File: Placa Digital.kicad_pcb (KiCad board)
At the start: 2 copper layers, 60 x 80 mm, 23 parts, among them J1 Entradas / Salidas, Q1 BC548, Q2 BC548, U1 EC11_Module, U2 Alimentación, U3 ST7920_Display, U4 10K

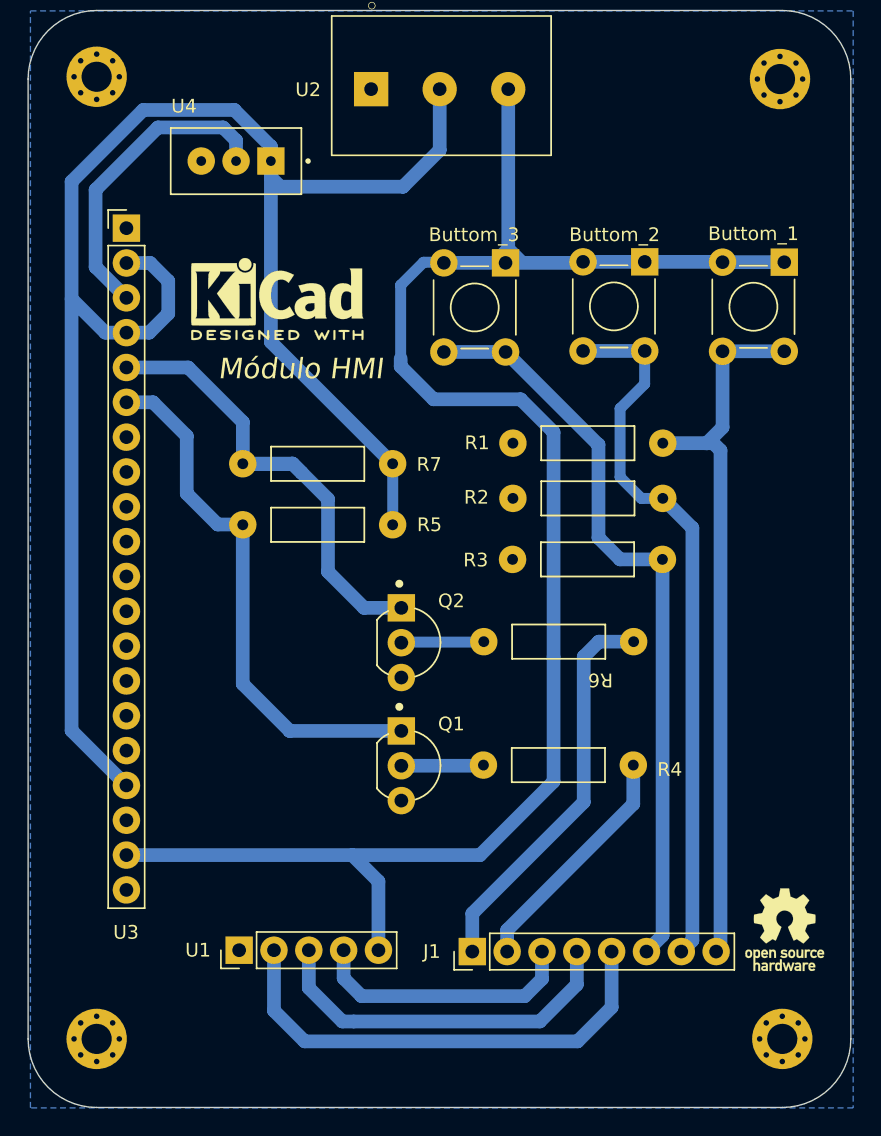
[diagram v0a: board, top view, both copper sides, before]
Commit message: Button changed
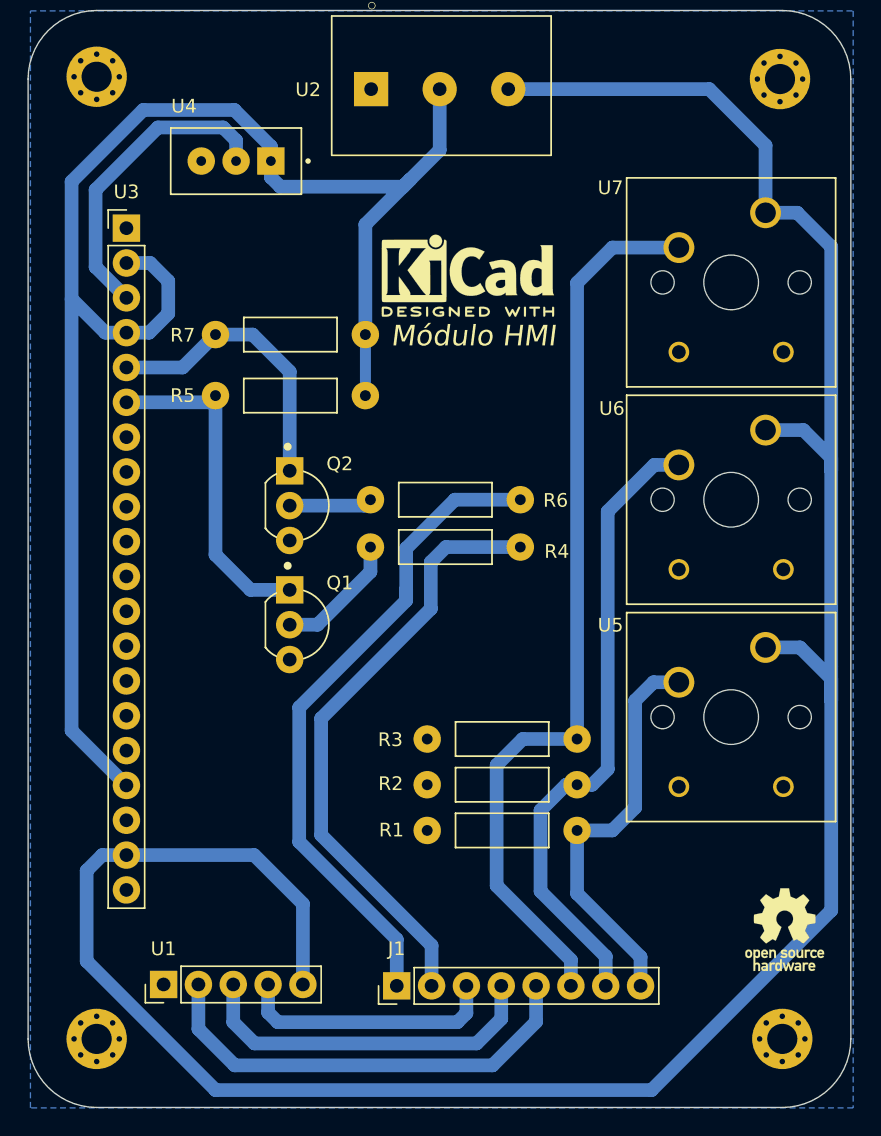
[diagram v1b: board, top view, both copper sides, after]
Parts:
- removed Buttom_1, Buttom_2, Buttom_3: -, CEDCp:Pulsador_4Pines
- added U5: MX1A-11NN, CEDCp:CHERRY_MX1A-11NN_SWITCH, F.Cu at (161.7, 110.8)
- added U6: MX1A-11NN, CEDCp:CHERRY_MX1A-11NN_SWITCH, F.Cu at (161.7, 95.0)
- added U7: MX1A-11NN, CEDCp:CHERRY_MX1A-11NN_SWITCH, F.Cu at (161.7, 79.1)
- moved R1 28.9 mm to (145.0, 119.1)
- moved R2 21.8 mm to (145.0, 115.8)
- moved R4 17.9 mm to (140.9, 98.4)
- moved R3 14.5 mm to (145.0, 112.4)
- moved REF** 14.0 mm to (142.5, 78.6)
- moved R6 13.2 mm to (140.9, 95.0)
- moved Q1 13.1 mm to (130.4, 104.1)
- moved Q2 12.9 mm to (130.4, 95.4)
- moved R5 9.63 mm to (129.6, 87.4)
- moved R7 9.63 mm to (129.6, 82.9)
- moved J1 6.05 mm to (137.3, 130.4)
- moved U1 6.05 mm to (120.3, 130.3)
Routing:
- net /toMicroC_Button1: track 67.7 -> 29.7 mm
- net Net-(Q1-Pad1): track 65.7 -> 36.4 mm
- net /fromMicroC_DisplaySCLK: track 17.4 -> 44.5 mm
- net Net-(Q2-Pad1): track 46.2 -> 21.3 mm
- net /fromMicroC_DisplaySID: track 31.5 -> 48.6 mm
- net +5V: track 175.3 -> 158.8 mm
- net +3V3: track 198.0 -> 187.3 mm
- net /toMicroC_Button2: track 56.9 -> 46.3 mm
- net Net-(Q1-Pad2): track 12.0 -> 9.29 mm
- net /toMicroC_Button3: track 69.4 -> 66.8 mm
- net /toMicroC_EncoderSignalA: track 35.1 -> 32.9 mm
- net /toMicroC_EncoderSignalB: track 26.8 -> 26.1 mm

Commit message: Last version
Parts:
- added H1: MountingHole, MountingHole:MountingHole_2.2mm_M2_Pad_Via, F.Cu at (142.3, 26.4)
- added H1: MountingHole, MountingHole:MountingHole_2.2mm_M2_Pad_Via, F.Cu at (40.1, 118.9)
- added H1: MountingHole, MountingHole:MountingHole_2.2mm_M2_Pad_Via, F.Cu at (142.6, 119.2)
- added H2: MountingHole, MountingHole:MountingHole_2.2mm_M2_Pad_Via, F.Cu at (90.0, 119.1)
- added H2: MountingHole, MountingHole:MountingHole_2.2mm_M2_Pad_Via, F.Cu at (192.1, 26.6)
- added H2: MountingHole, MountingHole:MountingHole_2.2mm_M2_Pad_Via, F.Cu at (192.5, 119.4)
- added H3: MountingHole, MountingHole:MountingHole_2.2mm_M2_Pad_Via, F.Cu at (192.6, 189.4)
- added H3: MountingHole, MountingHole:MountingHole_2.2mm_M2_Pad_Via, F.Cu at (192.3, 96.6)
- added H3: MountingHole, MountingHole:MountingHole_2.2mm_M2_Pad_Via, F.Cu at (90.1, 189.1)
- added H4: MountingHole, MountingHole:MountingHole_2.2mm_M2_Pad_Via, F.Cu at (142.6, 189.4)
- added H4: MountingHole, MountingHole:MountingHole_2.2mm_M2_Pad_Via, F.Cu at (142.3, 96.6)
- added H4: MountingHole, MountingHole:MountingHole_2.2mm_M2_Pad_Via, F.Cu at (40.1, 189.1)
- added J1: Entradas / Salidas, Connector_PinHeader_2.54mm:PinHeader_1x08_P2.54mm_Vertical, F.Cu at (62.0, 185.2)
- added J1: Entradas / Salidas, Connector_PinHeader_2.54mm:PinHeader_1x08_P2.54mm_Vertical, F.Cu at (164.2, 92.7)
- added J1: Entradas / Salidas, Connector_PinHeader_2.54mm:PinHeader_1x08_P2.54mm_Vertical, F.Cu at (164.5, 185.5)
- added Q1: BC548, CEDCp:BC548, F.Cu at (157.6, 159.2)
- added Q1: BC548, CEDCp:BC548, F.Cu at (157.2, 66.4)
- added Q1: BC548, CEDCp:BC548, F.Cu at (55.1, 158.9)
- added Q2: BC548, CEDCp:BC548, F.Cu at (55.1, 150.2)
- added Q2: BC548, CEDCp:BC548, F.Cu at (157.6, 150.5)
- added Q2: BC548, CEDCp:BC548, F.Cu at (157.2, 57.7)
- added R1: 10k, CEDCp:Resistencia_0,25W, F.Cu at (172.2, 174.2)
- added R1: 10k, CEDCp:Resistencia_0,25W, F.Cu at (171.8, 81.4)
- added R1: 10k, CEDCp:Resistencia_0,25W, F.Cu at (69.7, 173.9)
- added R2: 10k, CEDCp:Resistencia_0,25W, F.Cu at (171.8, 78.1)
- added R2: 10k, CEDCp:Resistencia_0,25W, F.Cu at (69.7, 170.5)
- added R2: 10k, CEDCp:Resistencia_0,25W, F.Cu at (172.2, 170.9)
- added R3: 10k, CEDCp:Resistencia_0,25W, F.Cu at (69.7, 167.2)
- added R3: 10k, CEDCp:Resistencia_0,25W, F.Cu at (172.2, 167.5)
- added R3: 10k, CEDCp:Resistencia_0,25W, F.Cu at (171.8, 74.7)
- added R4: 2k7, CEDCp:Resistencia_0,25W, F.Cu at (168.1, 153.5)
- added R4: 2k7, CEDCp:Resistencia_0,25W, F.Cu at (167.7, 60.7)
- added R4: 2k7, CEDCp:Resistencia_0,25W, F.Cu at (65.6, 153.2)
- added R5: 1k, CEDCp:Resistencia_0,25W, F.Cu at (54.3, 142.1)
- added R5: 1k, CEDCp:Resistencia_0,25W, F.Cu at (156.8, 142.5)
- added R5: 1k, CEDCp:Resistencia_0,25W, F.Cu at (156.4, 49.7)
- added R6: 2k7, CEDCp:Resistencia_0,25W, F.Cu at (167.7, 57.3)
- added R6: 2k7, CEDCp:Resistencia_0,25W, F.Cu at (65.6, 149.7)
- added R6: 2k7, CEDCp:Resistencia_0,25W, F.Cu at (168.1, 150.1)
- added R7: 1k, CEDCp:Resistencia_0,25W, F.Cu at (156.4, 45.2)
- added R7: 1k, CEDCp:Resistencia_0,25W, F.Cu at (54.3, 137.7)
- added R7: 1k, CEDCp:Resistencia_0,25W, F.Cu at (156.8, 138.0)
- added REF**: KiCad-Logo2_5mm_SilkScreen, Symbol:KiCad-Logo2_5mm_SilkScreen, F.Cu at (67.2, 133.4)
- added REF**: OSHW-Logo_5.7x6mm_SilkScreen, Symbol:OSHW-Logo_5.7x6mm_SilkScreen, F.Cu at (90.3, 181.1)
- added REF**: KiCad-Logo2_5mm_SilkScreen, Symbol:KiCad-Logo2_5mm_SilkScreen, F.Cu at (169.3, 40.9)
- added REF**: KiCad-Logo2_5mm_SilkScreen, Symbol:KiCad-Logo2_5mm_SilkScreen, F.Cu at (169.7, 133.7)
- added REF**: OSHW-Logo_5.7x6mm_SilkScreen, Symbol:OSHW-Logo_5.7x6mm_SilkScreen, F.Cu at (192.4, 88.6)
- added REF**: OSHW-Logo_5.7x6mm_SilkScreen, Symbol:OSHW-Logo_5.7x6mm_SilkScreen, F.Cu at (192.8, 181.4)
- added U1: EC11_Module, Connector_PinHeader_2.54mm:PinHeader_1x05_P2.54mm_Vertical, F.Cu at (45.0, 185.1)
- added U1: EC11_Module, Connector_PinHeader_2.54mm:PinHeader_1x05_P2.54mm_Vertical, F.Cu at (147.2, 92.6)
- added U1: EC11_Module, Connector_PinHeader_2.54mm:PinHeader_1x05_P2.54mm_Vertical, F.Cu at (147.5, 185.4)
- added U2: Alimentación, CEDCp:Bornera_1x3, F.Cu at (167.7, 120.1)
- added U2: Alimentación, CEDCp:Bornera_1x3, F.Cu at (65.1, 119.8)
- added U2: Alimentación, CEDCp:Bornera_1x3, F.Cu at (167.3, 27.3)
- added U3: ST7920_Display, Connector_PinHeader_2.54mm:PinHeader_1x20_P2.54mm_Vertical, F.Cu at (144.4, 37.5)
- added U3: ST7920_Display, Connector_PinHeader_2.54mm:PinHeader_1x20_P2.54mm_Vertical, F.Cu at (42.3, 129.9)
- added U3: ST7920_Display, Connector_PinHeader_2.54mm:PinHeader_1x20_P2.54mm_Vertical, F.Cu at (144.8, 130.3)
- added U4: 10K, CEDCp:Preset_Multivueltas_Vertical, F.Cu at (152.4, 32.6)
- added U4: 10K, CEDCp:Preset_Multivueltas_Vertical, F.Cu at (50.3, 125.0)
- added U4: 10K, CEDCp:Preset_Multivueltas_Vertical, F.Cu at (152.8, 125.4)
- added U5: MX1A-11NN, CEDCp:CHERRY_MX1A-11NN_SWITCH, B.Cu at (188.5, 73.1)
- added U5: MX1A-11NN, CEDCp:CHERRY_MX1A-11NN_SWITCH, B.Cu at (86.4, 165.6)
- added U5: MX1A-11NN, CEDCp:CHERRY_MX1A-11NN_SWITCH, B.Cu at (188.9, 165.9)
- added U6: MX1A-11NN, CEDCp:CHERRY_MX1A-11NN_SWITCH, B.Cu at (188.5, 57.3)
- added U6: MX1A-11NN, CEDCp:CHERRY_MX1A-11NN_SWITCH, B.Cu at (86.4, 149.7)
- added U6: MX1A-11NN, CEDCp:CHERRY_MX1A-11NN_SWITCH, B.Cu at (188.9, 150.1)
- added U7: MX1A-11NN, CEDCp:CHERRY_MX1A-11NN_SWITCH, B.Cu at (188.5, 41.4)
- added U7: MX1A-11NN, CEDCp:CHERRY_MX1A-11NN_SWITCH, B.Cu at (188.9, 134.2)
- added U7: MX1A-11NN, CEDCp:CHERRY_MX1A-11NN_SWITCH, B.Cu at (86.4, 133.9)
- U5, U6, U7: moved to B.Cu
- moved R4 85.0 mm to (64.8, 60.6)
- moved R6 85.0 mm to (64.8, 57.1)
- moved U5 85.0 mm to (85.6, 73.0), turned to 180 degrees
- moved U6 85.0 mm to (85.6, 57.1), turned to 180 degrees
- moved U7 85.0 mm to (85.6, 41.3), turned to 180 degrees
- moved H1 85.0 mm to (39.3, 26.3)
- moved H3 85.0 mm to (89.3, 96.4)
- moved H4 85.0 mm to (39.3, 96.4)
- moved J1 85.0 mm to (61.2, 92.6)
- moved Q1 85.0 mm to (54.3, 66.2)
- moved Q2 85.0 mm to (54.3, 57.5)
- moved R1 85.0 mm to (68.9, 81.2)
- moved R2 85.0 mm to (68.9, 77.9)
- moved R3 85.0 mm to (68.9, 74.6)
- moved R5 85.0 mm to (53.5, 49.5)
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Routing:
- net +3V3: track 187.3 -> 809.3 mm
- net +5V: track 158.8 -> 635.3 mm
- net /toMicroC_Button3: track 66.8 -> 301.2 mm
- net /toMicroC_Button2: track 46.3 -> 218.4 mm
- net /fromMicroC_DisplaySID: track 48.6 -> 194.3 mm
- net /fromMicroC_DisplaySCLK: track 44.5 -> 178.1 mm
- net /toMicroC_Button1: track 29.7 -> 152.2 mm
- net Net-(Q1-Pad1): track 36.4 -> 145.8 mm
- net /toMicroC_EncoderSignalA: track 32.9 -> 131.7 mm
- net Net-(U3-Pad3): track 28.5 -> 113.9 mm
- net /toMicroC_EncoderSignalB: track 26.1 -> 104.3 mm
- net Net-(Q2-Pad1): track 21.3 -> 85.1 mm
- net /toMicroC_EncoderButton: track 19.1 -> 76.3 mm
- net Net-(Q1-Pad2): track 9.29 -> 37.2 mm
- net Net-(Q2-Pad2): track 6.07 -> 24.3 mm
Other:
- board size 60 x 80 mm -> 163.3 x 173 mm
